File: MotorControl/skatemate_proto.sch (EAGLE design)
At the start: 104 parts, among them IC1 REG1117, Q1 IRF740, Q2 IRF740, Q3 IRF740, Q4 IRF740, Q5 IRF740, Q6 IRF740, U1 DRV8301DCAR

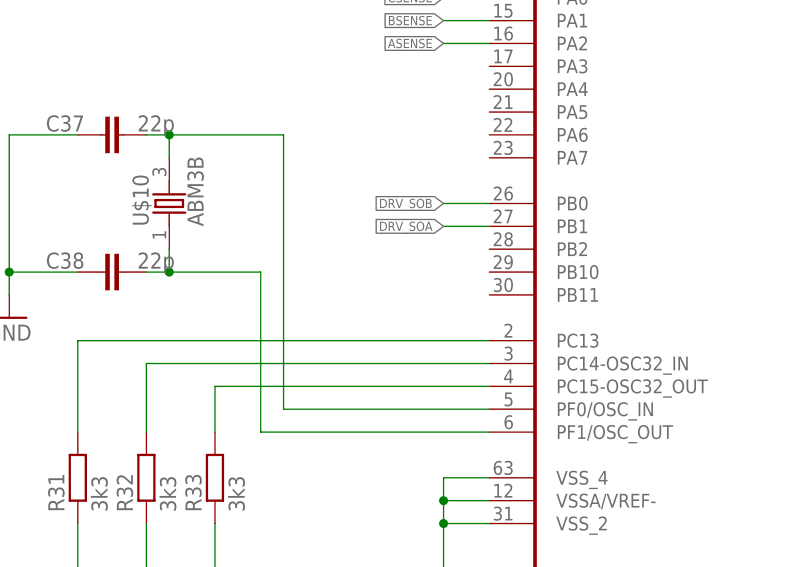
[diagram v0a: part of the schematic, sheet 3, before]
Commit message: added USART TX/RX labels
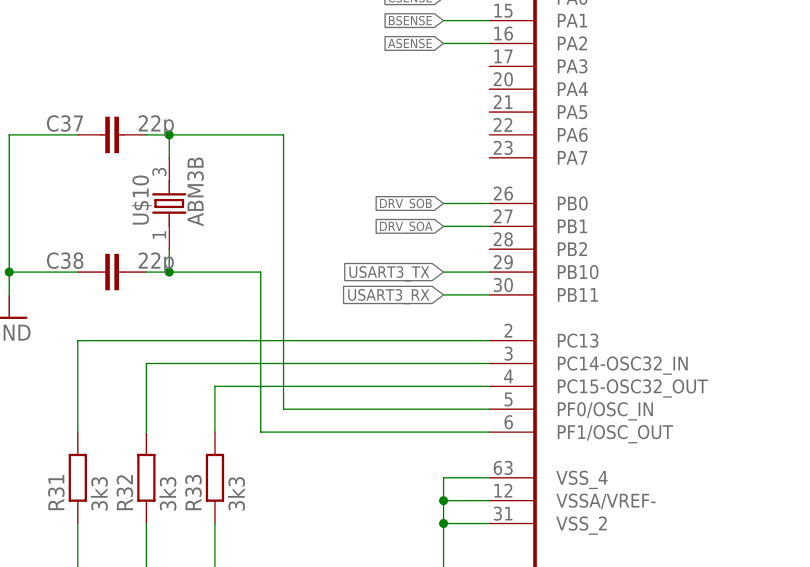
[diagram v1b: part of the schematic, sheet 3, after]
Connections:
- new net USART3_RX: U$3G$1.PB11
- new net USART3_TX: U$3G$1.PB10
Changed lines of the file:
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@@
+</segment>
+</net>
+<net name="USART3_RX" class="0">
+<segment>
+<pinref part="U$3" gate="G$1" pin="PB11"/>
+<wire x1="55.88" y1="91.44" x2="50.8" y2="91.44" width="0.1524" layer="91"/>
+<label x="50.8" y="91.44" size="1.27" layer="95" rot="R180" xref="yes"/>
+</segment>
+</net>
+<net name="USART3_TX" class="0">
+<segment>
+<pinref part="U$3" gate="G$1" pin="PB10"/>
+<wire x1="55.88" y1="93.98" x2="50.8" y2="93.98" width="0.1524" layer="91"/>
+<label x="50.8" y="93.98" size="1.27" layer="95" rot="R180" xref="yes"/>
 </segment>
 </net>
